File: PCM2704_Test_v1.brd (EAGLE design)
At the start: 54.1 x 35.4 mm, 50 parts, among them IC1 REG1117, IC2 REG1117, X1 USB-MB-S

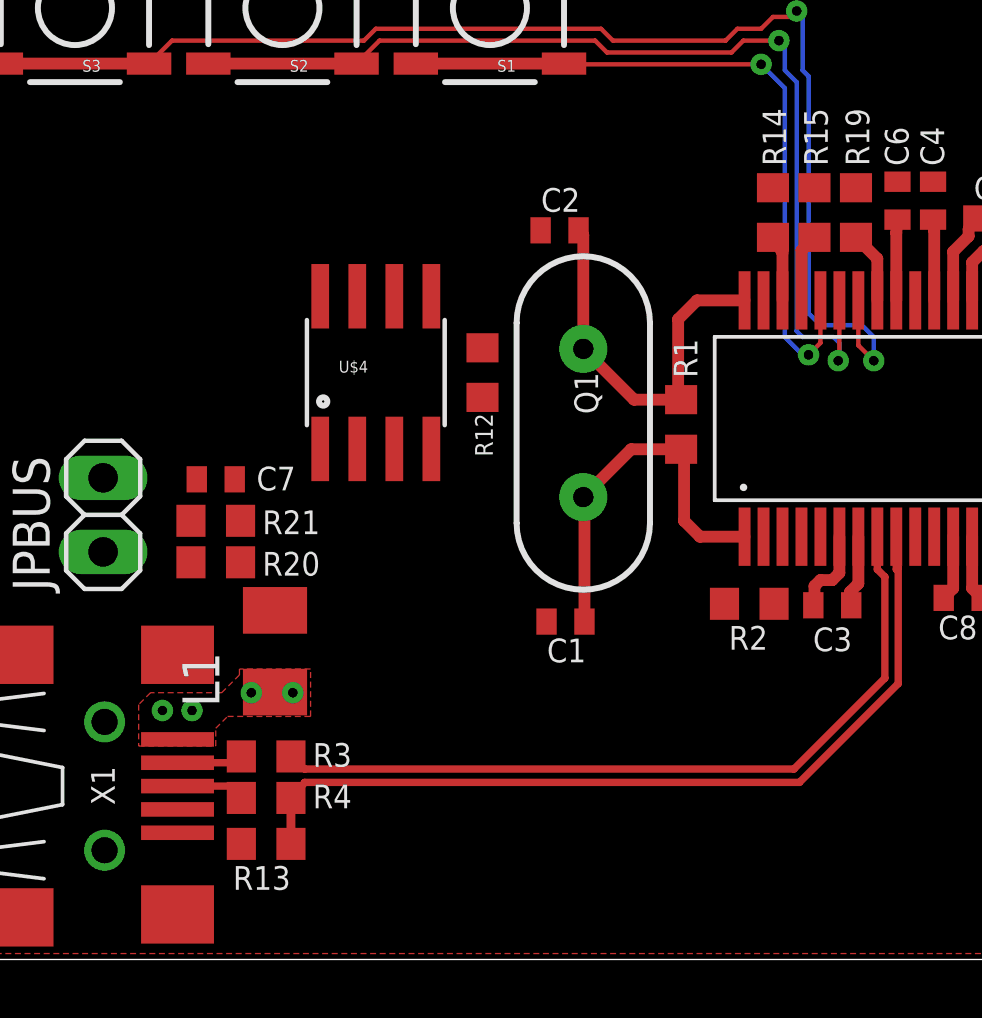
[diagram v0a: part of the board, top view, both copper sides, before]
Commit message: Small changes made
Wired up the SDA and SCL for the EEPROM. Also added a bypass cap to the
EEPROM.
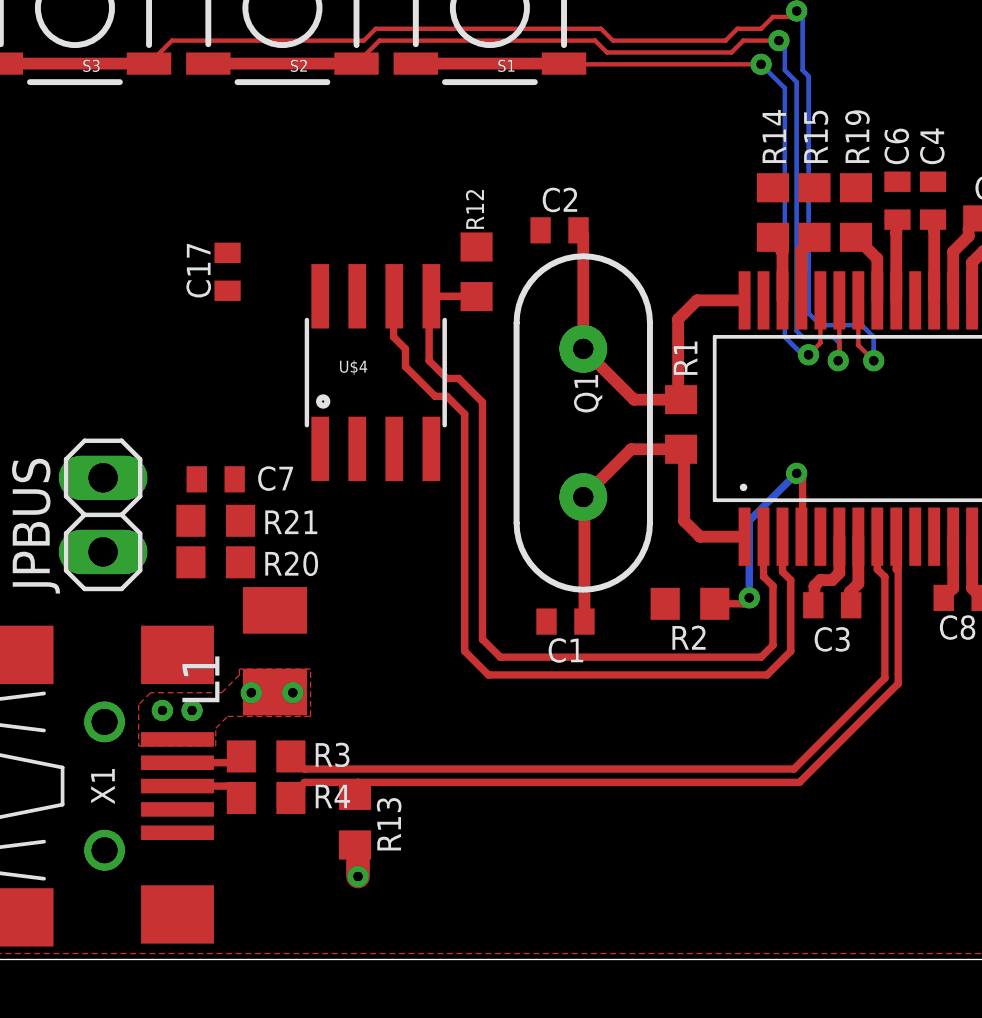
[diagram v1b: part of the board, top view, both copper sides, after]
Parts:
- added C17: 1u, rcl:C0402
- moved R12 3.46 mm to (19.9, 21.5), turned to 90 degrees
- moved R13 3.15 mm to (15.7, 2.74), turned to 270 degrees
- moved R2 2.03 mm to (27.2, 10.2)
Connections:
- net GND: now also C17.2
- net VDD: now also C17.1
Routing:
- net N$17: track 0.00 -> 29.3 mm
- net N$16: track 0.00 -> 28.6 mm
- net N$5: track 0.00 -> 8.48 mm, vias 0 -> 2
- net VDD: track 11.2 -> 12.4 mm, vias 0 -> 1
- net D_P: track 29.2 -> 28.2 mm
